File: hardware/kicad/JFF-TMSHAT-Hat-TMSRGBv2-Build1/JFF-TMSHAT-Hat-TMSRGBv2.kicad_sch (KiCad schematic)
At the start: 15 parts, among them J1 TMSRGB-OUT, J13 AV EXT, J5 RGB, U100 TMS-RGB

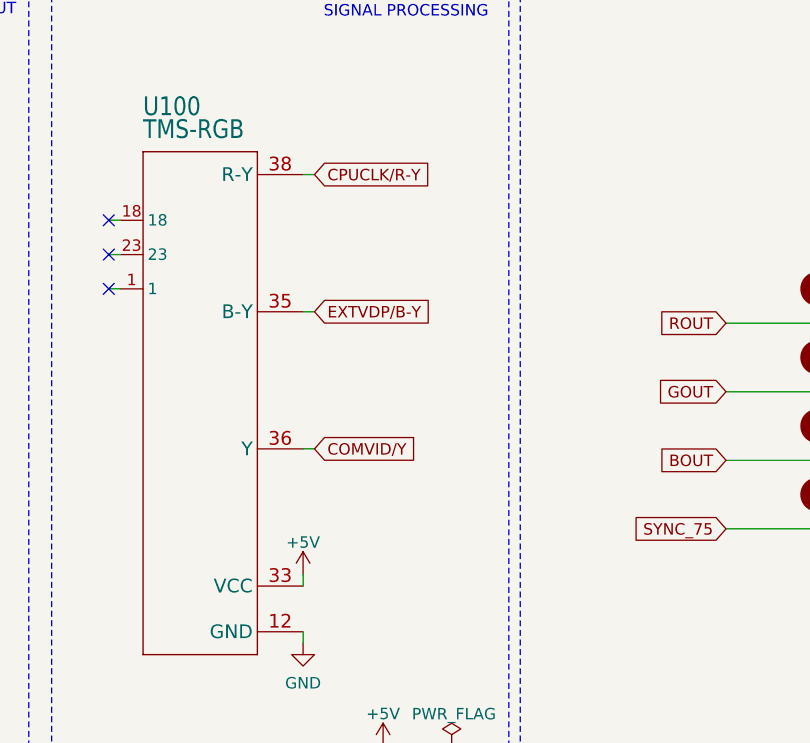
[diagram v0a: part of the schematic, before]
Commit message: tmshats: add missing Y,R-Y,B-Y resistors
Signed-off-by: Albert Herranz <albert_herranz@yahoo.es>
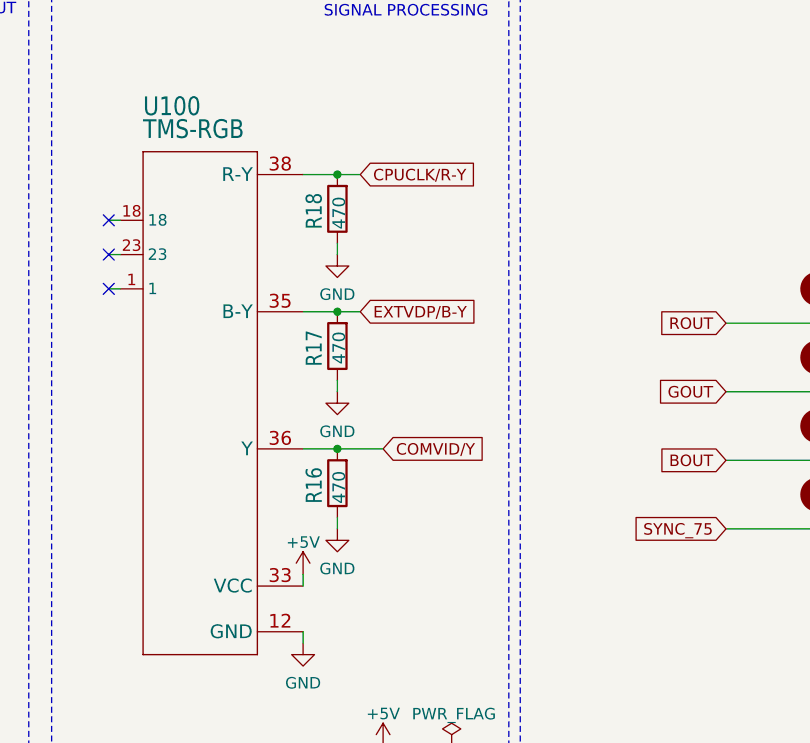
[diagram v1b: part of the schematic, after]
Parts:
- added R16, R17, R18: 470, Resistor_SMD:R_0805_2012Metric_Pad1.20x1.40mm_HandSolder, symbol Device:R
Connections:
- net COMVID/Y: now also R16.2
- net CPUCLK/R-Y: now also R18.2
- net EXTVDP/B-Y: now also R17.2
- net GND: now also R16.1, R17.1, R18.1
